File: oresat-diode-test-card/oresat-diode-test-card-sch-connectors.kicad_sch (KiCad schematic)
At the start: 5 parts, among them J6 J-SAMTEC-TFM-120-X1-XXX-D-RA

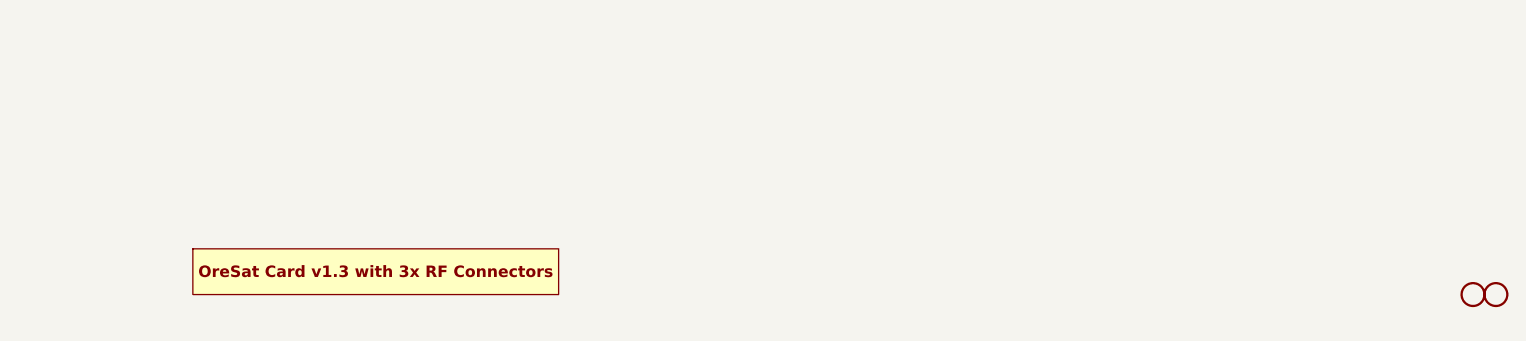
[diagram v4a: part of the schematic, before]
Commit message: second rought draft layout, fixed library issues
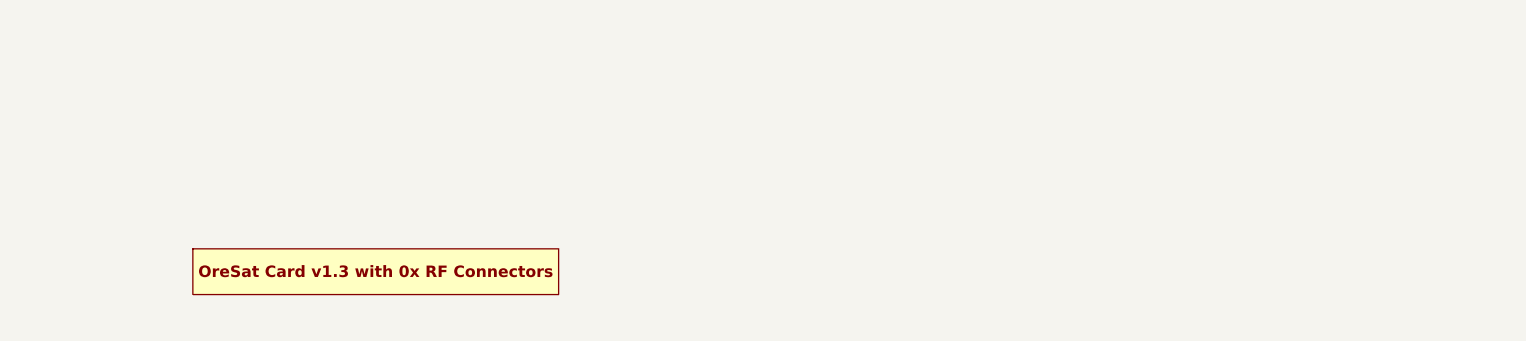
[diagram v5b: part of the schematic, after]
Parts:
- removed H2, H3: STAND-OFFTIGHT, oresat-proto-card:STAND-OFF-TIGHT, symbol oresat-proto-card-eagle-import:STAND-OFFTIGHT
- PCB1: symbol oresat-pcbs:ORESAT-CARD-V1.3-3RF -> oresat-pcbs:ORESAT-CARD-V1.3-0RF
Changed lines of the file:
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@@
-	)
-	(symbol
-		(lib_id "oresat-proto-card-eagle-import:STAND-OFFTIGHT")
-		(at 287.02 246.38 0)
-		(unit 1)
-		(exclude_from_sim no)
-		(in_bom yes)
-		(on_board yes)
-		(dnp no)
-		(property "Reference" "H3"
-			(at 287.02 246.38 0)
-			(effects
-				(font
-					(size 1.27 1.27)
-				)
-				(hide yes)
-			)
-		)
-		(property "Value" "STAND-OFFTIGHT"
-			(at 287.02 246.38 0)
-			(effects
-				(font
-					(size 1.27 1.27)
-				)
-				(hide yes)
-			)
-		)
-		(property "Footprint" "oresat-proto-card:STAND-OFF-TIGHT"
-			(at 287.02 246.38 0)
-			(effects
-				(font
-					(size 1.27 1.27)
-				)
-				(hide yes)
-			)
-		)
-		(property "Datasheet" ""
-			(at 287.02 246.38 0)
-			(effects
-				(font
-					(size 1.27 1.27)
-				)
-				(hide yes)
-			)
-		)
-		(property "Description" ""
-			(at 287.02 246.38 0)
-			(effects
-				(font
-					(size 1.27 1.27)
-				)
-				(hide yes)
-			)
-		)
-		(instances
-			(project "oresat-diode-test-card"
-				(path "/04d32576-d084-475b-9eac-d7f3fd9579d7/5e24a3e8-a65e-478d-b976-97cb63cc1885"
-					(reference "H3")
-					(unit 1)
-				)
-			)
-		)
 	)
 	(symbol
@@
 				(path "/04d32576-d084-475b-9eac-d7f3fd9579d7/5e24a3e8-a65e-478d-b976-97cb63cc1885"
 					(reference "J6")
-					(unit 1)
-				)
-			)
-		)
-	)
-	(symbol
-		(lib_id "oresat-proto-card-eagle-import:STAND-OFFTIGHT")
-		(at 284.48 246.38 0)
-		(unit 1)
-		(exclude_from_sim no)
-		(in_bom yes)
-		(on_board yes)
-		(dnp no)
-		(property "Reference" "H2"
-			(at 284.48 246.38 0)
-			(effects
-				(font
-					(size 1.27 1.27)
-				)
-				(hide yes)
-			)
-		)
-		(property "Value" "STAND-OFFTIGHT"
-			(at 284.48 246.38 0)
-			(effects
-				(font
-					(size 1.27 1.27)
-				)
-				(hide yes)
-			)
-		)
-		(property "Footprint" "oresat-proto-card:STAND-OFF-TIGHT"
-			(at 284.48 246.38 0)
-			(effects
-				(font
-					(size 1.27 1.27)
-				)
-				(hide yes)
-			)
-		)
-		(property "Datasheet" ""
-			(at 284.48 246.38 0)
-			(effects
-				(font
-					(size 1.27 1.27)
-				)
-				(hide yes)
-			)
-		)
-		(property "Description" ""
-			(at 284.48 246.38 0)
-			(effects
-				(font
-					(size 1.27 1.27)
-				)
-				(hide yes)
-			)
-		)
-		(instances
-			(project "oresat-diode-test-card"
-				(path "/04d32576-d084-475b-9eac-d7f3fd9579d7/5e24a3e8-a65e-478d-b976-97cb63cc1885"
-					(reference "H2")
 					(unit 1)
 				)
@@
 	)
 	(symbol
-		(lib_id "oresat-pcbs:ORESAT-CARD-V1.3-3RF")
+		(lib_id "oresat-pcbs:ORESAT-CARD-V1.3-0RF")
 		(at 162.56 243.84 0)
 		(unit 1)

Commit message: Added BOM
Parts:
- J6, JP2: DST (none) -> Digi-Key
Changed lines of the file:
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@@
+			)
+		)
+		(property "Sim.Device" ""
+			(at 73.66 96.52 0)
+			(effects
+				(font
+					(size 1.27 1.27)
+				)
+				(hide yes)
+			)
+		)
+		(property "Sim.Pins" ""
+			(at 73.66 96.52 0)
+			(effects
+				(font
+					(size 1.27 1.27)
+				)
+				(hide yes)
+			)
+		)
+		(property "Sim.Type" ""
+			(at 73.66 96.52 0)
+			(effects
+				(font
+					(size 1.27 1.27)
+				)
+				(hide yes)
+			)
+		)
+		(property "DST" "Digi-Key"
+			(at 73.66 96.52 0)
+			(effects
+				(font
+					(size 1.27 1.27)
+				)
+				(hide yes)
 			)
 		)
@@
 			)
 		)
+		(property "Sim.Device" ""
+			(at 195.58 129.54 0)
+			(effects
+				(font
+					(size 1.27 1.27)
+				)
+				(hide yes)
+			)
+		)
+		(property "Sim.Pins" ""
+			(at 195.58 129.54 0)
+			(effects
+				(font
+					(size 1.27 1.27)
+				)
+				(hide yes)
+			)
+		)
+		(property "Sim.Type" ""
+			(at 195.58 129.54 0)
+			(effects
+				(font
+					(size 1.27 1.27)
+				)
+				(hide yes)
+			)
+		)
+		(property "DST" "Digi-Key"
+			(at 195.58 129.54 0)
+			(effects
+				(font
+					(size 1.27 1.27)
+				)
+				(hide yes)
+			)
+		)
 		(pin "1"
 		)
@@
 			(at 162.56 243.84 0)
 			(effects
+				(font
+					(size 1.27 1.27)
+				)
+				(hide yes)
+			)
+		)
+		(property "Sim.Device" ""
+			(at 162.56 243.84 0)
+			(effects
+				(font
+					(size 1.27 1.27)
+				)
+				(hide yes)
+			)
+		)
+		(property "Sim.Pins" ""
+			(at 162.56 243.84 0)
+			(effects
+				(font
+					(size 1.27 1.27)
+				)
+				(hide yes)
+			)
+		)
+		(property "Sim.Type" ""
+			(at 162.56 243.84 0)
+			(effects

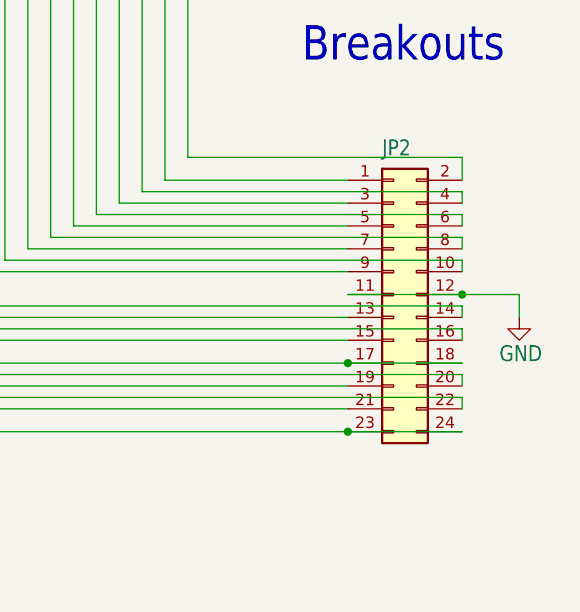
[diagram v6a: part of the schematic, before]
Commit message: BOM changes! Now up to date.
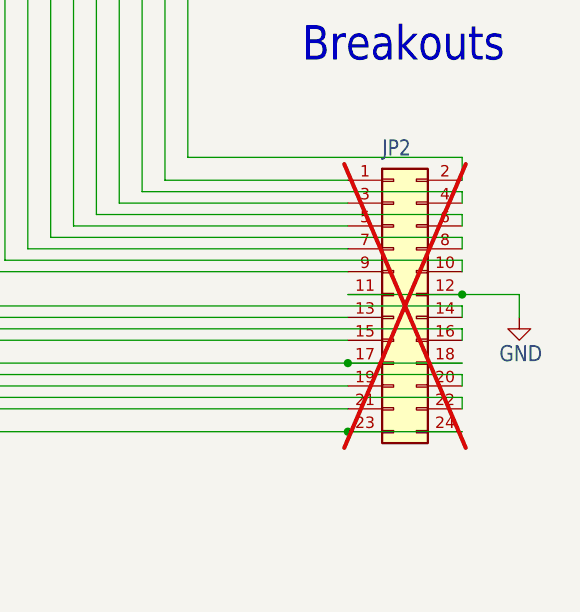
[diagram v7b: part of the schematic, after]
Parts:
- J6: DIS Digi-Key -> (none); DPN SAM10145-ND -> SAM10145-ND; DST Digi-Key -> DigiKey
- JP2: value PINHD-2X5 -> PINHD-2X12; DIS Digi-Key -> (none); DPN 609-3243-ND -> N/A; DST Digi-Key -> N/A; MFR Amphenol -> N/A; MPN 67997-410HLF -> N/A; now not fitted; now left out of the parts list
- PCB1: DPN (none) -> N/A; DST (none) -> N/A; MFR (none) -> N/A; MPN (none) -> N/A
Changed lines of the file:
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@@
 			)
 		)
-		(property "Datasheet" ""
-			(at 73.66 96.52 0)
-			(effects
-				(font
-					(size 1.27 1.27)
-				)
-				(hide yes)
-			)
-		)
-		(property "Description" ""
-			(at 73.66 96.52 0)
-			(effects
-				(font
-					(size 1.27 1.27)
-				)
-				(hide yes)
-			)
-		)
-		(property "DIS" "Digi-Key"
-			(at 73.66 96.52 0)
-			(effects
-				(font
-					(size 1.27 1.27)
-				)
-				(justify left bottom)
-				(hide yes)
-			)
-		)
-		(property "DPN" "SAM10145-ND "
+		(property "Datasheet" "https://mm.digikey.com/Volume0/opasdata/d220001/medias/docus/6129/tfm-1xx-xx-x-dh-xx-mkt.pdf"
+			(at 73.66 96.52 0)
+			(effects
+				(font
+					(size 1.27 1.27)
+				)
+				(hide yes)
+			)
+		)
+		(property "Description" "Connector Header Through Hole, Right Angle 40 position 0.050\" (1.27mm)"
+			(at 73.66 96.52 0)
+			(effects
+				(font
+					(size 1.27 1.27)
+				)
+				(hide yes)
+			)
+		)
+		(property "DPN" "SAM10145-ND"
 			(at 73.66 96.52 0)
 			(effects
@@
 			)
 		)
-		(property "Sim.Device" ""
-			(at 73.66 96.52 0)
-			(effects
-				(font
-					(size 1.27 1.27)
-				)
-				(hide yes)
-			)
-		)
-		(property "Sim.Pins" ""
-			(at 73.66 96.52 0)
-			(effects
-				(font
-					(size 1.27 1.27)
-				)
-				(hide yes)
-			)
-		)
-		(property "Sim.Type" ""
-			(at 73.66 96.52 0)
-			(effects
-				(font
-					(size 1.27 1.27)
-				)
-				(hide yes)
-			)
-		)
-		(property "DST" "Digi-Key"
+		(property "DST" "DigiKey"
 			(at 73.66 96.52 0)
 			(effects
@@
 		(unit 1)
 		(exclude_from_sim no)
-		(in_bom yes)
+		(in_bom no)
 		(on_board yes)
-		(dnp no)
+		(dnp yes)
 		(property "Reference" "JP2"
 			(at 194.31 114.3 0)
@@
 			)
 		)
-		(property "Value" "PINHD-2X5"
+		(property "Value" "PINHD-2X12"
 			(at 189.23 139.7 0)
 			(effects
@@
 			)
 		)
-		(property "Description" ""
-			(at 195.58 129.54 0)
-			(effects
-				(font
-					(size 1.27 1.27)
-				)
-				(hide yes)
-			)
-		)
-		(property "DIS" "Digi-Key"
-			(at 195.58 129.54 0)
-			(effects
-				(font
-					(size 1.27 1.27)
-				)
-				(justify left bottom)
-				(hide yes)
-			)
-		)
-		(property "DPN" "609-3243-ND"
-			(at 195.58 129.54 0)
-			(effects
-				(font
-					(size 1.27 1.27)
-				)
-				(justify left bottom)
-				(hide yes)
-			)
-		)
-		(property "MFR" "Amphenol "
-			(at 195.58 129.54 0)
-			(effects
-				(font
-					(size 1.27 1.27)
-				)
-				(justify left bottom)
-				(hide yes)
-			)
-		)
-		(property "MPN" "67997-410HLF"
-			(at 195.58 129.54 0)
-			(effects
-				(font
-					(size 1.27 1.27)
-				)
-				(justify left bottom)
-				(hide yes)
-			)
-		)
-		(property "Sim.Device" ""
-			(at 195.58 129.54 0)
-			(effects
-				(font
-					(size 1.27 1.27)
-				)
-				(hide yes)
-			)
-		)
-		(property "Sim.Pins" ""
-			(at 195.58 129.54 0)
-			(effects
-				(font
-					(size 1.27 1.27)
-				)
-				(hide yes)
-			)
-		)
-		(property "Sim.Type" ""
-			(at 195.58 129.54 0)
-			(effects
-				(font
-					(size 1.27 1.27)
-				)
-				(hide yes)
-			)
-		)
-		(property "DST" "Digi-Key"
+		(property "Description" "N/A"
+			(at 195.58 129.54 0)
+			(effects
+				(font
+					(size 1.27 1.27)
+				)
+				(hide yes)
+			)
+		)
+		(property "DPN" "N/A"
+			(at 195.58 129.54 0)
+			(effects
+				(font
+					(size 1.27 1.27)
+				)
+				(justify left bottom)
+				(hide yes)
+			)
+		)
+		(property "MFR" "N/A"
+			(at 195.58 129.54 0)
+			(effects
+				(font
+					(size 1.27 1.27)
+				)
+				(justify left bottom)
+				(hide yes)
+			)
+		)
+		(property "MPN" "N/A"
+			(at 195.58 129.54 0)
+			(effects
+				(font
+					(size 1.27 1.27)
+				)
+				(justify left bottom)
+				(hide yes)
+			)
+		)
+		(property "DST" "N/A"
 			(at 195.58 129.54 0)
 			(effects
@@
 			)
 		)
-		(property "Datasheet" ""
-			(at 162.56 243.84 0)
-			(effects
-				(font
-					(size 1.27 1.27)
-				)
-				(hide yes)
-			)
-		)
-		(property "Description" ""
-			(at 162.56 243.84 0)
-			(effects
-				(font
-					(size 1.27 1.27)
-				)
-				(hide yes)
-			)
-		)
-		(property "Sim.Device" ""
-			(at 162.56 243.84 0)
-			(effects
-				(font
-					(size 1.27 1.27)
-				)
-				(hide yes)
-			)
-		)
-		(property "Sim.Pins" ""
-			(at 162.56 243.84 0)
-			(effects
-				(font
-					(size 1.27 1.27)
-				)
-				(hide yes)
-			)
-		)
-		(property "Sim.Type" ""
-			(at 162.56 243.84 0)
-			(effects
+		(property "Datasheet" "N/A"
+			(at 162.56 243.84 0)
+			(effects
+				(font
+					(size 1.27 1.27)
+				)
+				(hide yes)
+			)
+		)
+		(property "Description" "N/A"
+			(at 162.56 243.84 0)
+			(effects
+				(font
+					(size 1.27 1.27)
+				)
+				(hide yes)
+			)
+		)
+		(property "DPN" "N/A"
+			(at 162.56 243.84 0)
+			(effects
+				(font
+					(size 1.27 1.27)
+				)
+				(hide yes)
+			)
+		)
+		(property "DST" "N/A"
+			(at 162.56 243.84 0)
+			(effects
+				(font
+					(size 1.27 1.27)
+				)
+				(hide yes)
+			)
+		)
+		(property "MFR" "N/A"
+			(at 162.56 243.84 0)
+			(effects
+				(font
+					(size 1.27 1.27)
+				)
+				(hide yes)
+			)
+		)
+		(property "MPN" "N/A"
+			(at 162.56 243.84 0)
+			(effects
